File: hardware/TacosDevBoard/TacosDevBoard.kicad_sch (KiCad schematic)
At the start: 5 parts, among them J1 Conn_01x15_Socket, J2 Conn_01x15_Socket, J3 Conn_01x08_Socket, J4 Conn_01x08_Socket

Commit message: Add buzzer to Dev Board
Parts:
- added BZ1: Buzzer, Buzzer_Beeper:Buzzer_12x9.5RM7.6, symbol Device:Buzzer
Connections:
- net D13: now also BZ1.1 (+)
- net GND: now also BZ1.2 (-)
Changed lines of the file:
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@@
+		)
+	)
+	(global_label "D13"
+		(shape bidirectional)
+		(at 190.5 95.25 180)
+		(fields_autoplaced yes)
+		(effects
+			(font
+				(size 0.762 0.762)
+			)
+			(justify right)
+		)
+		(property "Intersheetrefs" "${INTERSHEET_REFS}"
+			(at 185.8284 95.25 0)
+			(effects
+				(font
+					(size 1.27 1.27)
+				)
+				(justify right)
+				(hide yes)
+			)
 		)
 	)
@@
 	)
 	(symbol
+		(lib_id "Device:Buzzer")
+		(at 193.04 97.79 0)
+		(unit 1)
+		(exclude_from_sim no)
+		(in_bom yes)
+		(on_board yes)
+		(dnp no)
+		(fields_autoplaced yes)
+		(property "Reference" "BZ1"
+			(at 196.85 96.5199 0)
+			(effects
+				(font
+					(size 1.27 1.27)
+				)
+				(justify left)
+			)
+		)
+		(property "Value" "Buzzer"
+			(at 196.85 99.0599 0)
+			(effects
+				(font
+					(size 1.27 1.27)
+				)
+				(justify left)
+			)
+		)
+		(property "Footprint" "Buzzer_Beeper:Buzzer_12x9.5RM7.6"
+			(at 192.405 95.25 90)
+			(effects
+				(font
+					(size 1.27 1.27)
+				)
+				(hide yes)
+			)
+		)
+		(property "Datasheet" "~"
+			(at 192.405 95.25 90)
+			(effects
+				(font
+					(size 1.27 1.27)
+				)
+				(hide yes)
+			)
+		)
+		(property "Description" "Buzzer, polarized"
+			(at 193.04 97.79 0)
+			(effects
+				(font
+					(size 1.27 1.27)
+				)
+				(hide yes)
+			)
+		)
+		(pin "1"
+		)
+		(pin "2"
+		)
+		(instances
+			(project ""
+				(path "/e7c9e0c0-2f0c-494d-99d8-ec46463e3278"
+					(reference "BZ1")
+					(unit 1)
+				)
+			)
+		)
+	)
+	(symbol
 		(lib_id "power:+5V")
 		(at 217.17 119.38 90)
@@
 					(unit 1)
 				)
+			)
+		)
+	)
+	(symbol
+		(lib_id "power:GND")
+		(at 190.5 100.33 270)
+		(unit 1)
+		(exclude_from_sim no)
+		(in_bom yes)
+		(on_board yes)
+		(dnp no)
+		(property "Reference" "#PWR010"
+			(at 184.15 100.33 0)
+			(effects
+				(font
+					(size 1.27 1.27)
+				)
+				(hide yes)
+			)
+		)
+		(property "Value" "GND"
+			(at 186.69 100.3301 90)
+			(effects
+				(font
+					(size 1.27 1.27)
+				)
+				(justify right)
+			)
+		)
+		(property "Footprint" ""
+			(at 190.5 100.33 0)
+			(effects
+				(font
+					(size 1.27 1.27)
+				)
+				(hide yes)
+			)
+		)
+		(property "Datasheet" ""
+			(at 190.5 100.33 0)
+			(effects
+				(font
+					(size 1.27 1.27)
+				)
+				(hide yes)
+			)
+		)
+		(property "Description" "Power symbol creates a global label with name \"GND\" , ground"
+			(at 190.5 100.33 0)
+			(effects
+				(font
+					(size 1.27 1.27)
+				)
+				(hide yes)
+			)
+		)
+		(pin "1"
+		)
+		(instances
+			(project "TacosDevBoard"
+				(path "/e7c9e0c0-2f0c-494d-99d8-ec46463e3278"
+					(reference "#PWR010")
+					(unit 1)
+				)

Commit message: finished mega pcb
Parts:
- removed A1: Arduino_Nano_v3.x, Module:Arduino_Nano, symbol MCU_Module:Arduino_Nano_v3.x
- removed J1, J2: Conn_01x15_Socket, Connector_PinSocket_2.54mm:PinSocket_1x15_P2.54mm_Vertical, symbol Connector:Conn_01x15_Socket
- added IC2_COMM1: Conn_01x08_Socket, Connector_PinSocket_2.54mm:PinSocket_1x08_P2.54mm_Vertical, symbol Connector:Conn_01x08_Socket
- added J1, J2, J3, J4, J5: Conn_01x08_Socket, Connector_PinHeader_2.54mm:PinHeader_1x08_P2.54mm_Vertical, symbol Connector:Conn_01x08_Socket
- added J7: Conn_02x17_Counter_Clockwise, Connector_PinHeader_2.54mm:PinHeader_2x17_P2.54mm_Vertical, symbol Connector_Generic:Conn_02x17_Counter_Clockwise
- added J9: Conn_01x10_Pin, Connector_PinHeader_2.54mm:PinHeader_1x10_P2.54mm_Vertical, symbol Connector:Conn_01x10_Pin
- renumbered J4 to PWM1, J3 to SELECT1
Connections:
- net RX0: now also IC2_COMM1.2 (Pin_2), J5.1 (Pin_1)
- net TX1: now also IC2_COMM1.3 (Pin_3), J4.4 (Pin_4)
- net A0 renamed ~D6
- net ~D6: now also J5.7 (Pin_7)
- net A1 renamed ~D7
- net ~D7: now also J5.8 (Pin_8)
- net A2 renamed ~D8
- net ~D8: now also J9.1 (Pin_1)
- net A3 renamed ~D9
- net ~D9: now also J9.2 (Pin_2)
- net D10 renamed ~D4
- net ~D4: now also J5.5 (Pin_5)
- net D11 renamed ~D5
- net ~D5: now also J5.6 (Pin_6)
- net D2 renamed D22
- net D22: now also J7.2 (Pin_2)
- net D3 renamed D24
- net D24: now also J7.3 (Pin_3)
- net D4 renamed D26
- net D26: now also J7.4 (Pin_4)
- net D5 renamed D28
- net D28: now also J7.5 (Pin_5)
- net D6 renamed D30
- net D30: now also J7.6 (Pin_6)
- net D7 renamed D32
- net D32: now also J7.7 (Pin_7)
- net D8 renamed ~D2
- net ~D2: now also J5.3 (Pin_3)
- net D9 renamed ~D3
- net ~D3: now also J5.4 (Pin_4)
- new net RX1: IC2_COMM1.4 (Pin_4), J4.3 (Pin_3)
- new net RX2: IC2_COMM1.6 (Pin_6), J4.5 (Pin_5)
- new net RX3: IC2_COMM1.8 (Pin_8), J4.7 (Pin_7)
- new net TX0: IC2_COMM1.1 (Pin_1), J5.2 (Pin_2)
- new net TX2: IC2_COMM1.5 (Pin_5), J4.6 (Pin_6)
- new net TX3: IC2_COMM1.7 (Pin_7), J4.8 (Pin_8)
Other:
- note added: "Arduino Mega Pinout"
- moved on the sheet: BZ1, PWM1, SELECT1

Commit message: finished dev board
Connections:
- net D13 is gone; now on net D52: BZ1.1 (+)
- net +5V: now also J3.5 (Pin_5)
- net GND: now also J3.6 (Pin_6), J3.7 (Pin_7)
- net VIN: now also J3.8 (Pin_8)
- net +3.3V: now reaches J3.4 (Pin_4)
- net D52: now reaches J7.17 (Pin_17)

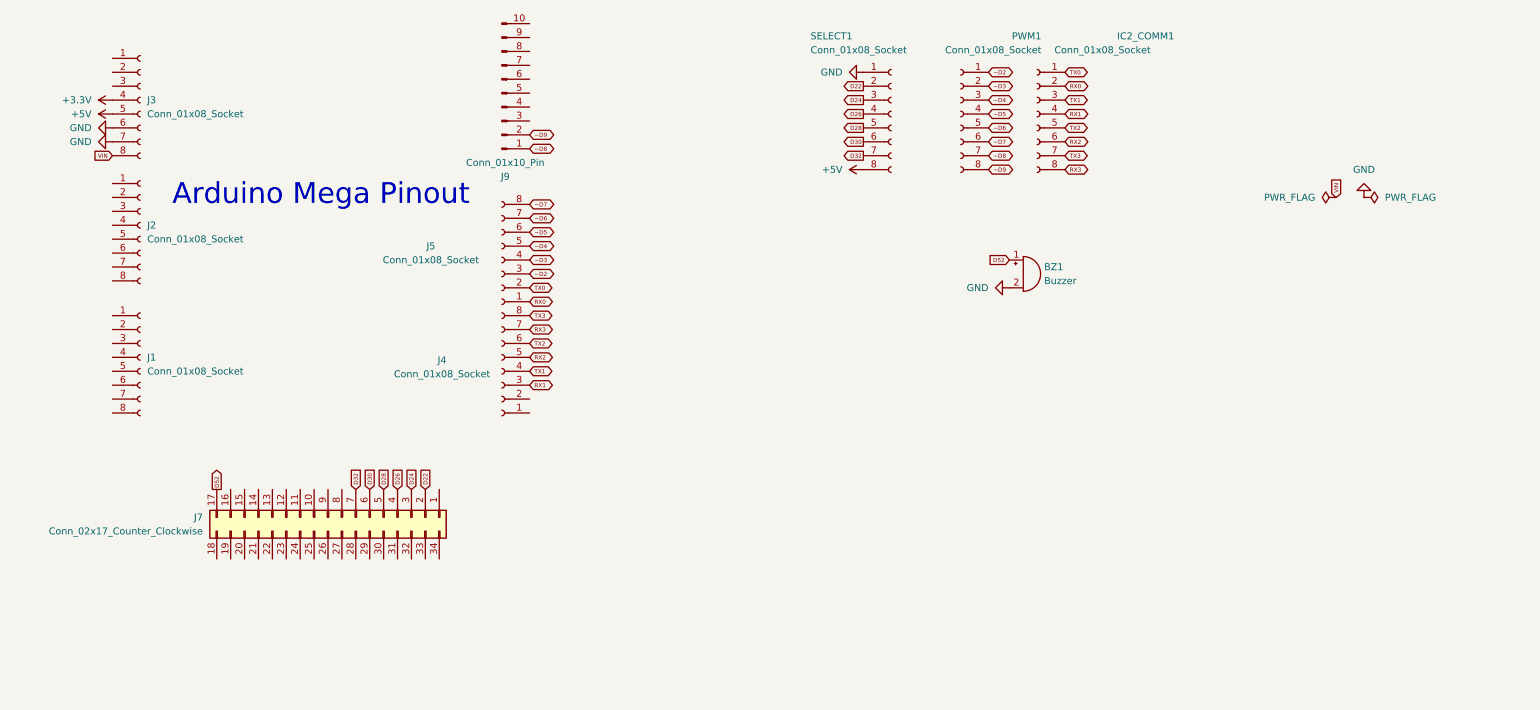
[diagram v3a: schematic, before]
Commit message: applied noconnects to unused dev board pins
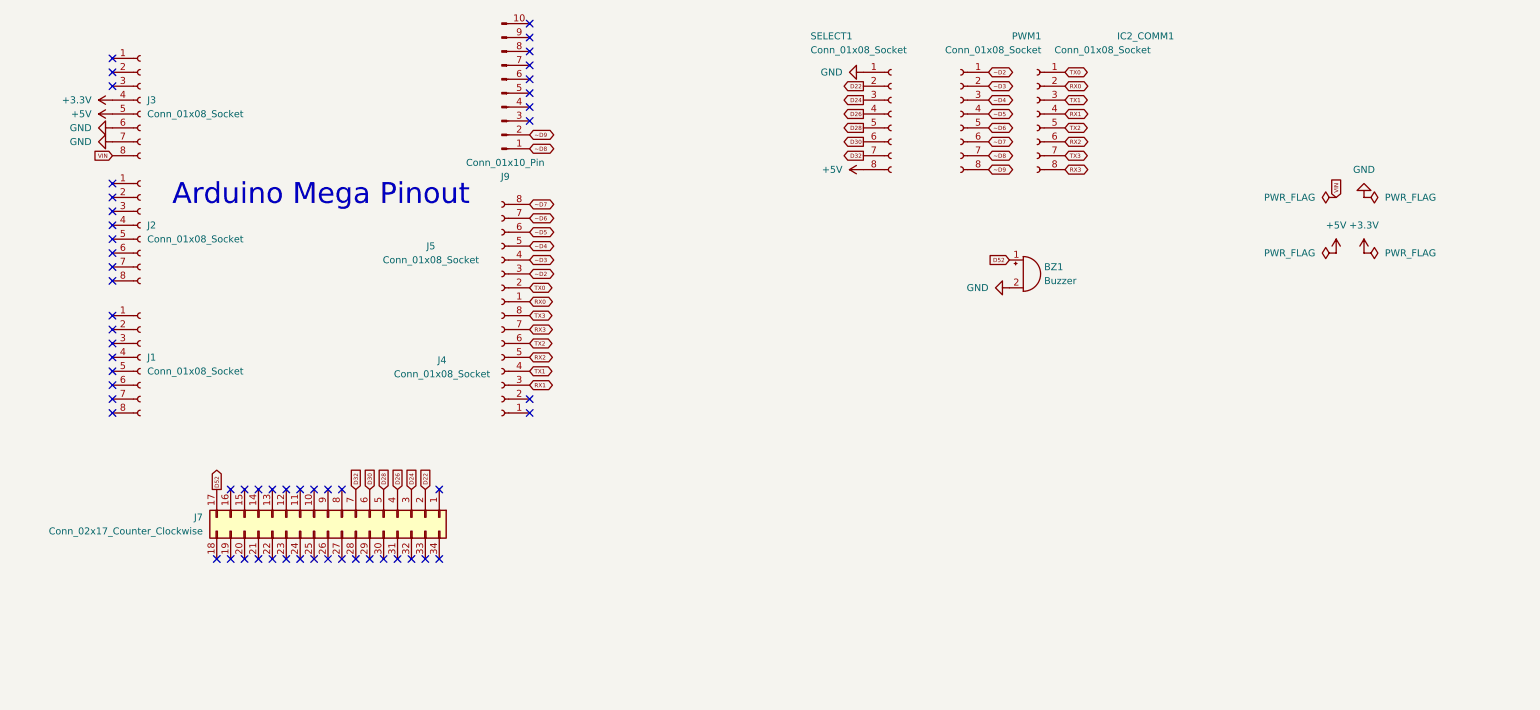
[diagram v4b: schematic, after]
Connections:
- no-connect marks 0 -> 56

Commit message: started adding SD card
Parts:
- added J6: Micro_SD_Card_Det2, Connector_Card:microSD_HC_Molex_104031-0811, symbol Connector:Micro_SD_Card_Det2
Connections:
- net at J7.18 (Pin_18): now also J6.6 (VSS)
- net at J7.26 (Pin_26): now also J6.9 (DET_B)
- net at J7.27 (Pin_27): now also J6.10 (DET_A)
- net at J7.28 (Pin_28): now also J6.8 (DAT1)
- net at J7.29 (Pin_29): now also J6.7 (DAT0)
- net at J7.30 (Pin_30): now also J6.5 (CLK)
- net at J7.31 (Pin_31): now also J6.3 (CMD)
- net at J7.32 (Pin_32): now also J6.2 (DAT3/CD)
- net at J7.33 (Pin_33): now also J6.1 (DAT2)
- net at J7.34 (Pin_34): now also J6.4 (VDD)
- no-connect marks 56 -> 47
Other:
- moved on the sheet: J7

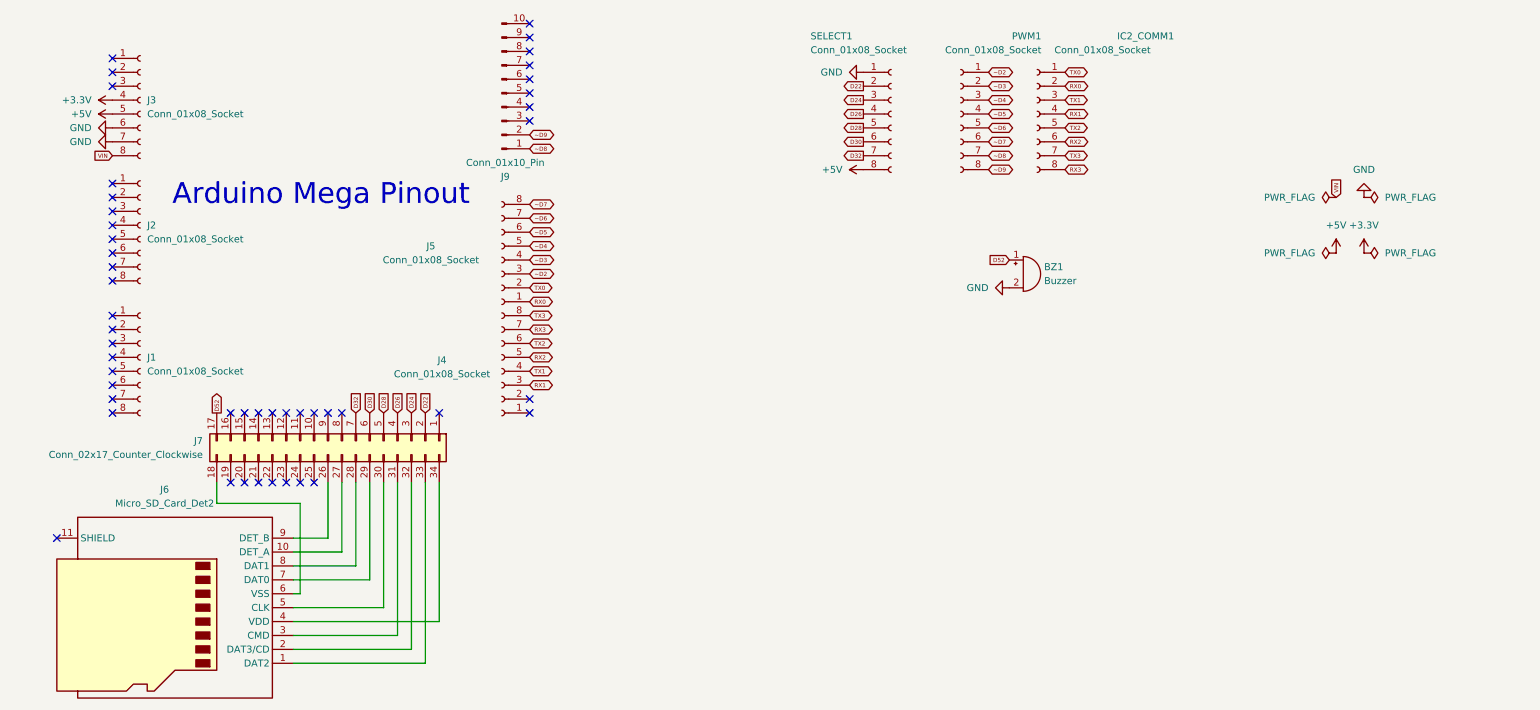
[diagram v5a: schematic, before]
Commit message: added sd card to dev board
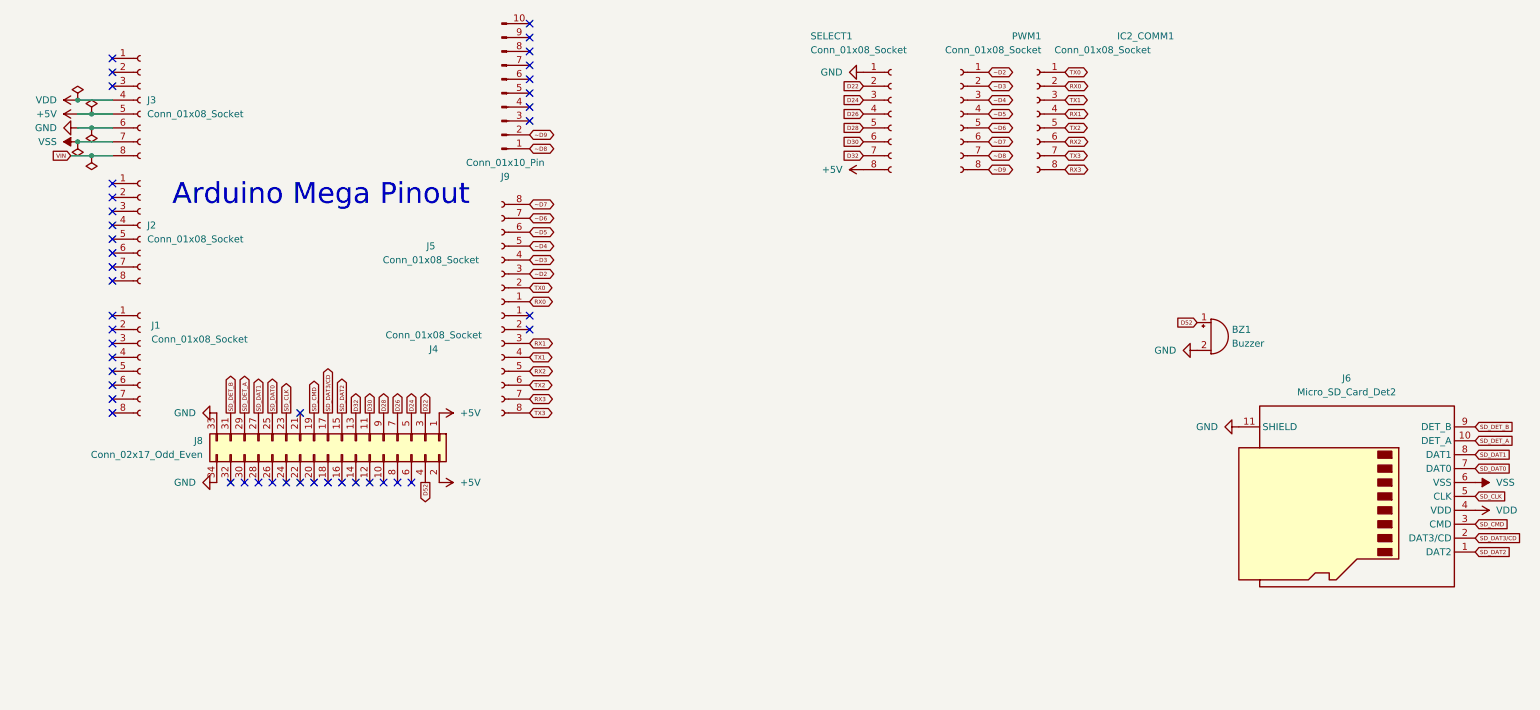
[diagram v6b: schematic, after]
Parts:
- removed J7: Conn_02x17_Counter_Clockwise, Connector_PinHeader_2.54mm:PinHeader_2x17_P2.54mm_Vertical, symbol Connector_Generic:Conn_02x17_Counter_Clockwise
- added J8: Conn_02x17_Odd_Even, Connector_PinHeader_2.54mm:PinHeader_2x17_P2.54mm_Vertical, symbol Connector_Generic:Conn_02x17_Odd_Even
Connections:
- net +3.3V is gone; now on net VDD: J3.4 (Pin_4)
- net +5V: now also J8.1 (Pin_1), J8.2 (Pin_2)
- net D22: now also J8.3 (Pin_3)
- net D24: now also J8.5 (Pin_5)
- net D26: now also J8.7 (Pin_7)
- net D28: now also J8.9 (Pin_9)
- net D30: now also J8.11 (Pin_11)
- net D32: now also J8.13 (Pin_13)
- net D52: now also J8.4 (Pin_4)
- net GND: now also J6.11 (SHIELD), J8.33 (Pin_33), J8.34 (Pin_34); no longer J3.7 (Pin_7)
- net SD_DAT2: now reaches J6.1 (DAT2)
- net SD_DAT2: now also J8.15 (Pin_15)
- net SD_DET_A: now reaches J6.10 (DET_A)
- net SD_DET_A: now also J8.29 (Pin_29)
- net SD_DAT3/CD: now reaches J6.2 (DAT3/CD)
- net SD_DAT3/CD: now also J8.17 (Pin_17)
- net SD_CMD: now reaches J6.3 (CMD)
- net SD_CMD: now also J8.19 (Pin_19)
- net VDD: now reaches J6.4 (VDD)
- net SD_CLK: now reaches J6.5 (CLK)
- net SD_CLK: now also J8.23 (Pin_23)
- net VSS: now reaches J6.6 (VSS)
- net VSS: now also J3.7 (Pin_7)
- net SD_DAT0: now reaches J6.7 (DAT0)
- net SD_DAT0: now also J8.25 (Pin_25)
- net SD_DAT1: now reaches J6.8 (DAT1)
- net SD_DAT1: now also J8.27 (Pin_27)
- net SD_DET_B: now reaches J6.9 (DET_B)
- net SD_DET_B: now also J8.31 (Pin_31)
- no-connect marks 47 -> 44
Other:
- moved on the sheet: BZ1, J4, J6

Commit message: finished dev board rewire
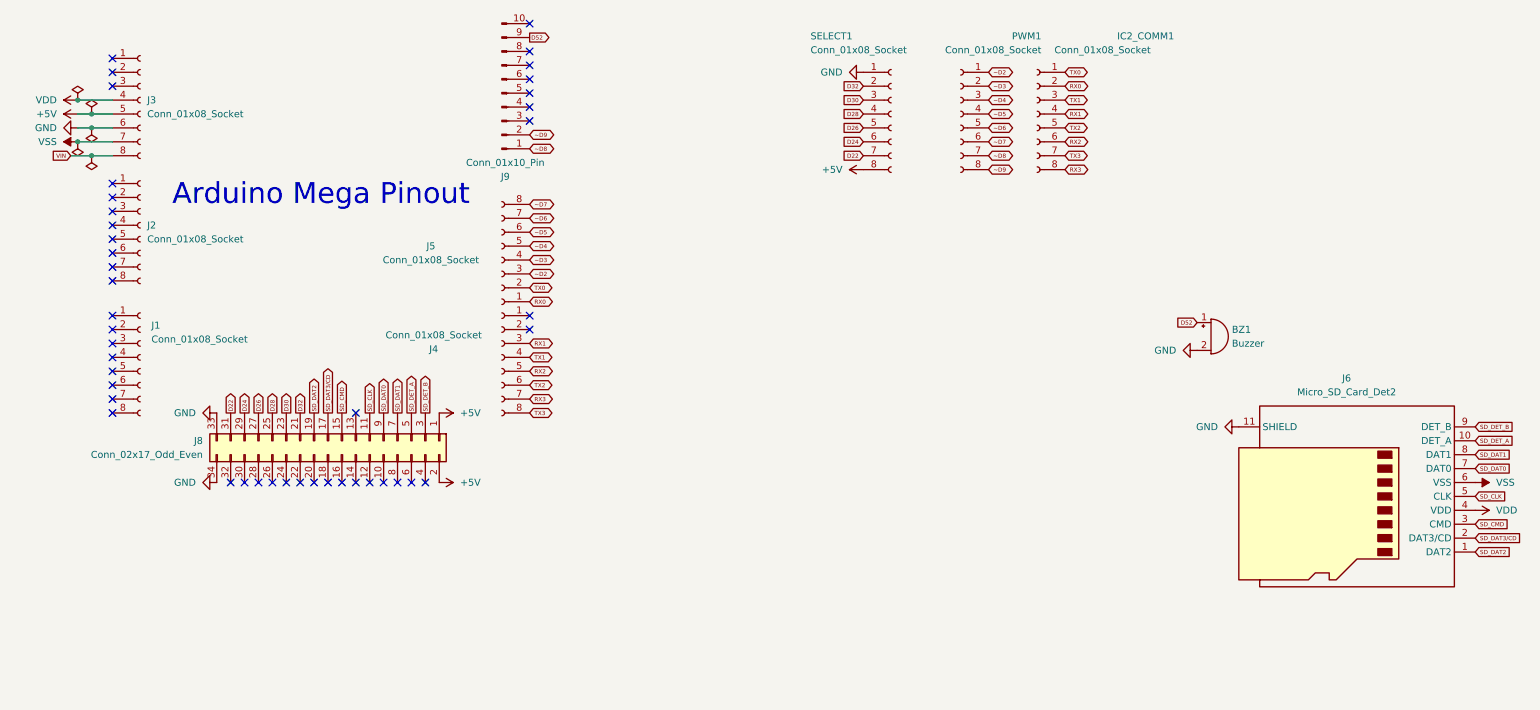
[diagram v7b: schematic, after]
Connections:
- net D22: now also J8.31 (Pin_31), SELECT1.7 (Pin_7); no longer J8.3 (Pin_3), SELECT1.2 (Pin_2)
- net D24: now also J8.29 (Pin_29), SELECT1.6 (Pin_6); no longer J8.5 (Pin_5), SELECT1.3 (Pin_3)
- net D26: now also J8.27 (Pin_27), SELECT1.5 (Pin_5); no longer J8.7 (Pin_7), SELECT1.4 (Pin_4)
- net D28: now also J8.25 (Pin_25), SELECT1.4 (Pin_4); no longer J8.9 (Pin_9), SELECT1.5 (Pin_5)
- net D30: now also J8.23 (Pin_23), SELECT1.3 (Pin_3); no longer J8.11 (Pin_11), SELECT1.6 (Pin_6)
- net D32: now also J8.21 (Pin_21), SELECT1.2 (Pin_2); no longer J8.13 (Pin_13), SELECT1.7 (Pin_7)
- net D52: now also J9.9 (Pin_9); no longer J8.4 (Pin_4)
- net SD_CLK: now also J8.11 (Pin_11); no longer J8.23 (Pin_23)
- net SD_CMD: now also J8.15 (Pin_15); no longer J8.19 (Pin_19)
- net SD_DAT0: now also J8.9 (Pin_9); no longer J8.25 (Pin_25)
- net SD_DAT1: now also J8.7 (Pin_7); no longer J8.27 (Pin_27)
- net SD_DAT2: now also J8.19 (Pin_19); no longer J8.15 (Pin_15)
- net SD_DET_A: now also J8.5 (Pin_5); no longer J8.29 (Pin_29)
- net SD_DET_B: now also J8.3 (Pin_3); no longer J8.31 (Pin_31)
